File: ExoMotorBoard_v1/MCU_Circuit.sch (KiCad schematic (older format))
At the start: 12 parts, among them IC1 DSPIC33FJ128MC802-I_SP, J4 Conn_01x06_Male, SW1 SW_Push_Dual

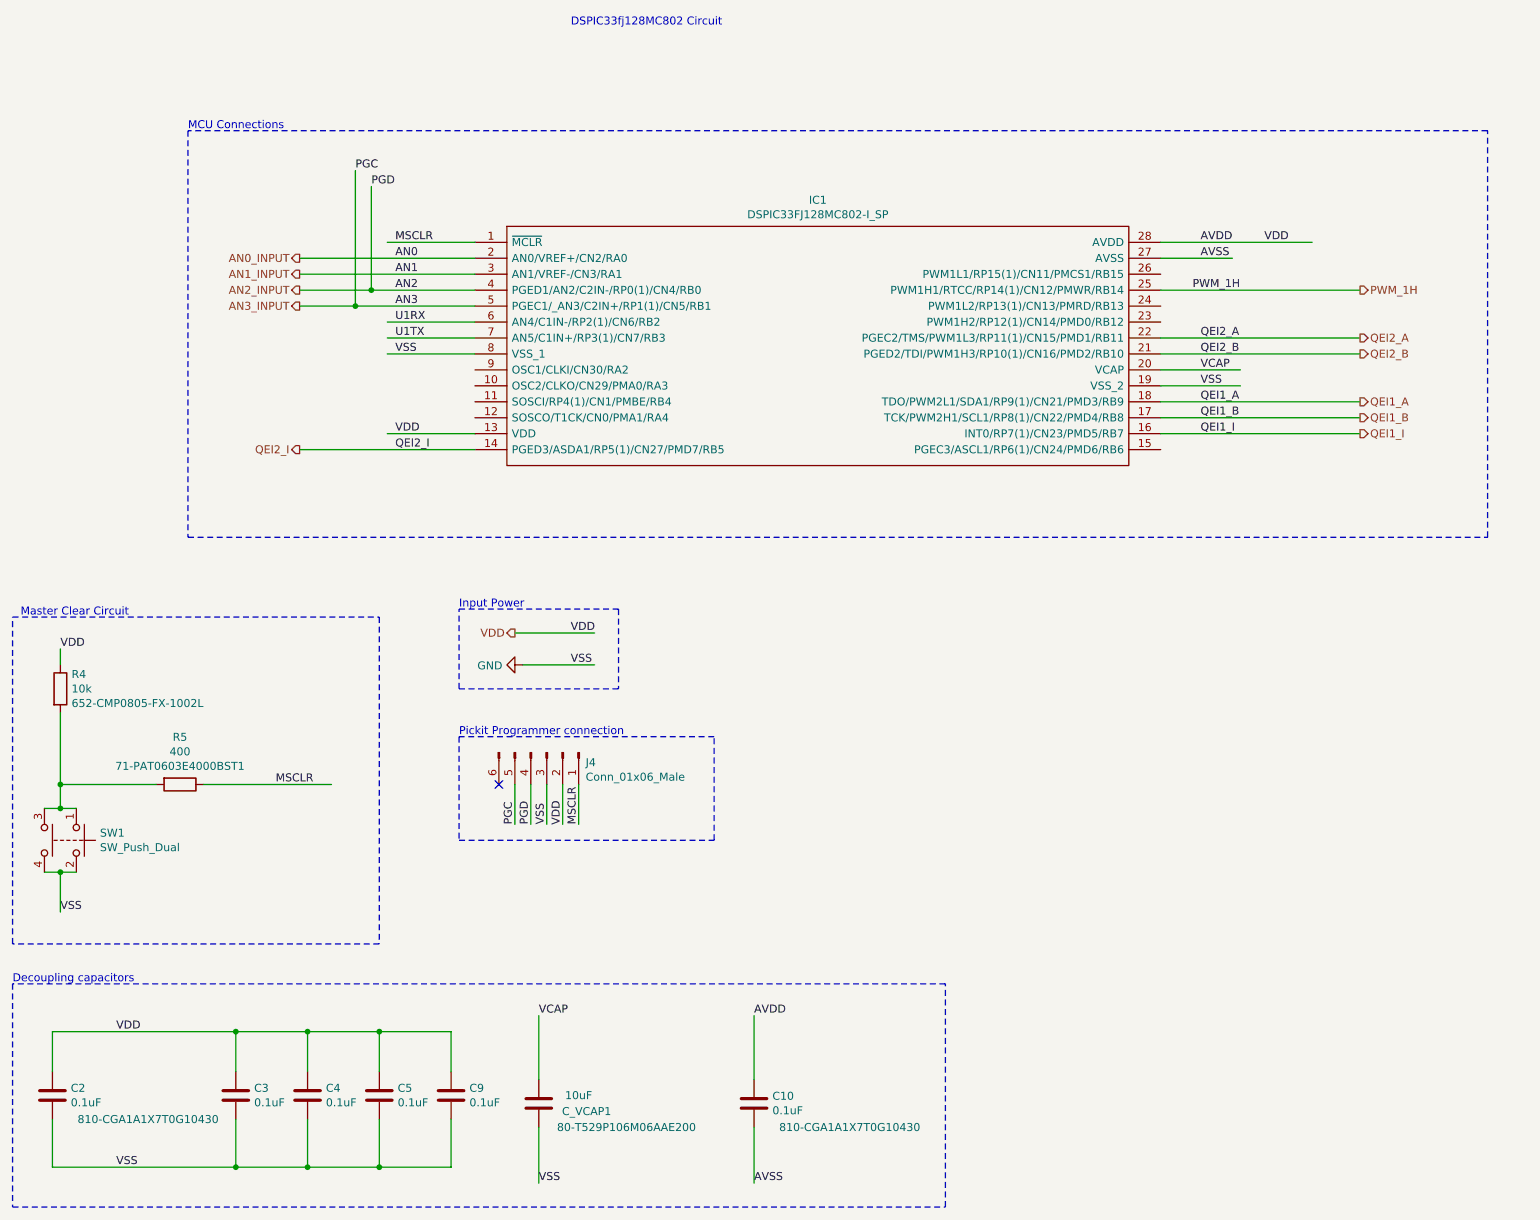
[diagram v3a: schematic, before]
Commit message: updated pins in the MCU circuit
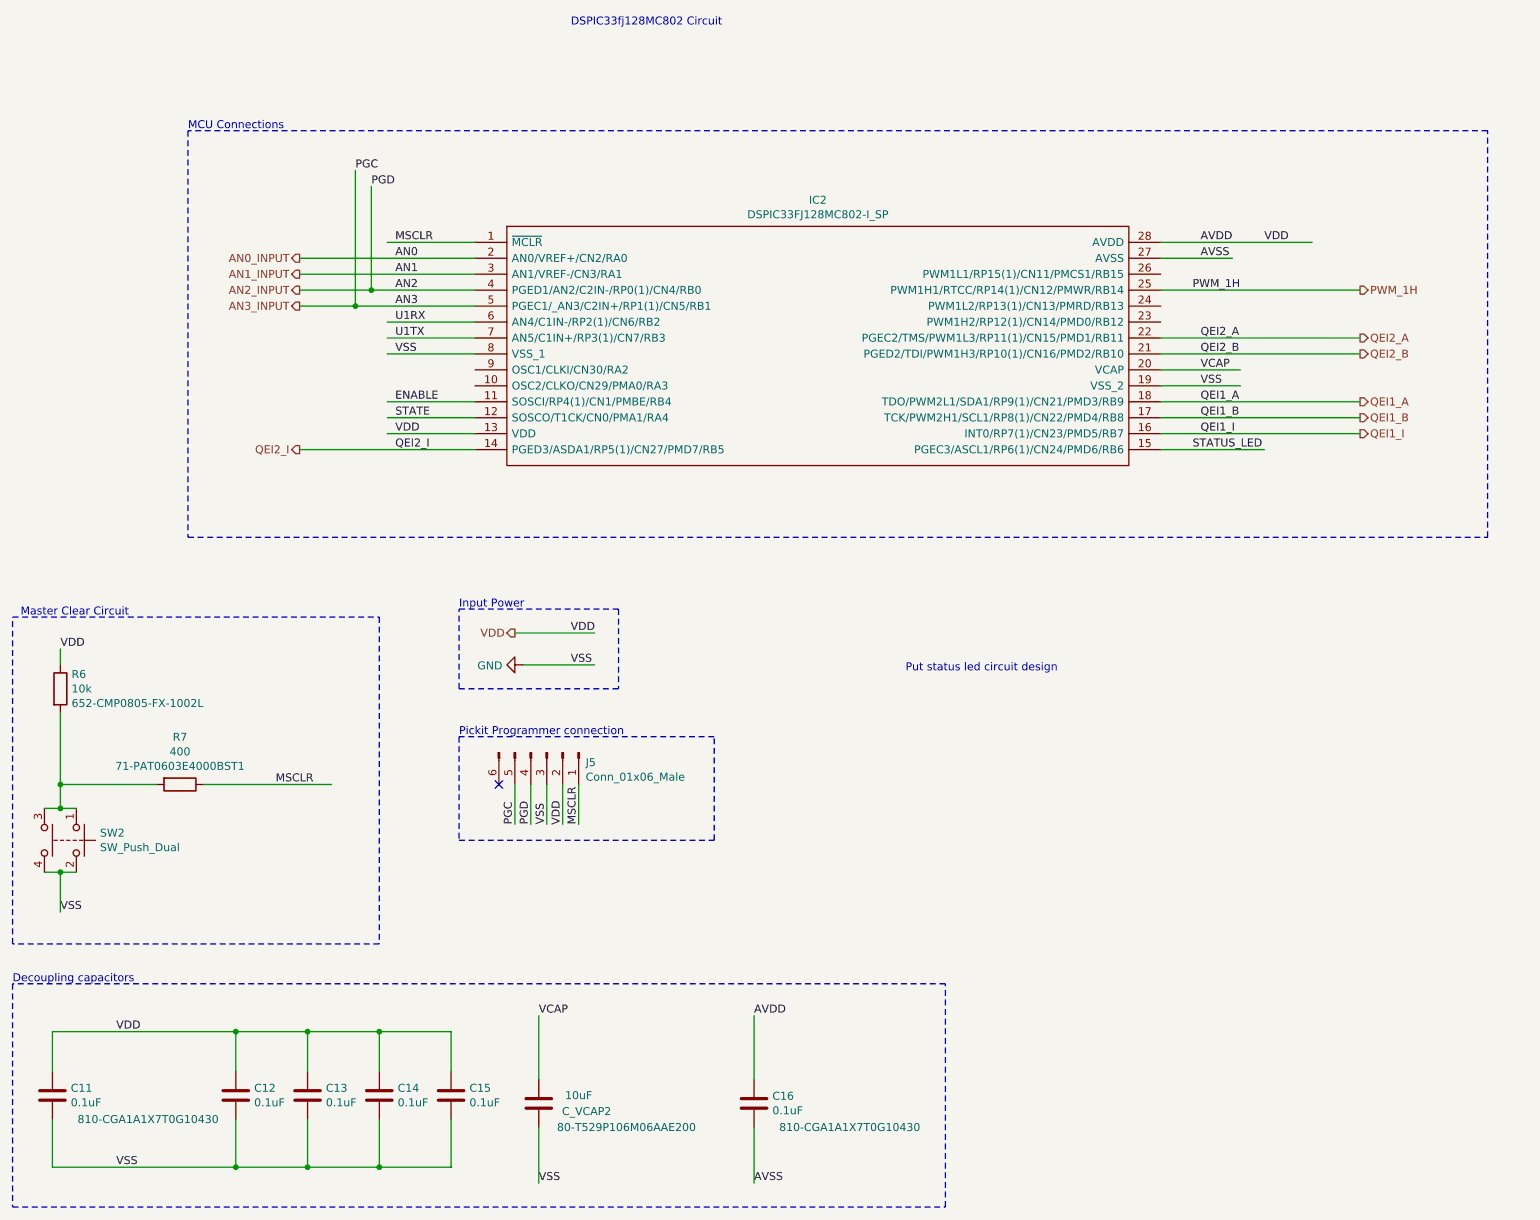
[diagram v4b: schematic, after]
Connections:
- net labels added: ENABLE, STATE, STATUS_LED
- wire segments 63 -> 66
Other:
- note added: "Put status led circuit design\n"
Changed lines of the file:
@@
 $Descr A4 11693 8268
 encoding utf-8
-Sheet 7 8
+Sheet 8 8
 Title ""
 Date ""
@@
 AR Path="/610E570F/610E8175" Ref="IC1"  Part="1"
 AR Path="/6118F320/610E8175" Ref="IC2"  Part="1"
-F 0 "IC1" H 5850 1815 50  0000 C CNN
+F 0 "IC2" H 5850 1815 50  0000 C CNN
 F 1 "DSPIC33FJ128MC802-I_SP" H 5850 1724 50  0000 C CNN
 F 2 "DSPIC33FJ128MC802-I_SP:DIP794W56P254L3486H508Q28N" H 7850 1650 50  0001 L CNN
@@
 AR Path="/610E570F/610E817B" Ref="C_VCAP1"  Part="1"
 AR Path="/6118F320/610E817B" Ref="C_VCAP2"  Part="1"
-F 0 "C_VCAP1" H 3800 7000 50  0000 C CNN
+F 0 "C_VCAP2" H 3800 7000 50  0000 C CNN
 F 1 "10uF" H 3850 6900 50  0000 C CNN
 F 2 "Capacitor_SMD:C_0805_2012Metric_Pad1.18x1.45mm_HandSolder" H 4138 6800 50  0001 C CNN
@@
 AR Path="/610E570F/610E818F" Ref="C2"  Part="1"
 AR Path="/6118F320/610E818F" Ref="C11"  Part="1"
-F 0 "C2" H 1165 6946 50  0000 L CNN
+F 0 "C11" H 1165 6946 50  0000 L CNN
 F 1 "0.1uF" H 1165 6855 50  0000 L CNN
 F 2 "Capacitor_SMD:C_0805_2012Metric_Pad1.18x1.45mm_HandSolder" H 1088 6750 50  0001 C CNN
@@
 AR Path="/610E570F/61167308" Ref="C3"  Part="1"
 AR Path="/6118F320/61167308" Ref="C12"  Part="1"
-F 0 "C3" H 2315 6946 50  0000 L CNN
+F 0 "C12" H 2315 6946 50  0000 L CNN
 F 1 "0.1uF" H 2315 6855 50  0000 L CNN
 F 2 "Capacitor_SMD:C_0805_2012Metric_Pad1.18x1.45mm_HandSolder" H 2238 6750 50  0001 C CNN
@@
 AR Path="/610E570F/611683F9" Ref="C4"  Part="1"
 AR Path="/6118F320/611683F9" Ref="C13"  Part="1"
-F 0 "C4" H 2765 6946 50  0000 L CNN
+F 0 "C13" H 2765 6946 50  0000 L CNN
 F 1 "0.1uF" H 2765 6855 50  0000 L CNN
 F 2 "Capacitor_SMD:C_0805_2012Metric_Pad1.18x1.45mm_HandSolder" H 2688 6750 50  0001 C CNN
@@
 AR Path="/610E570F/61168710" Ref="C5"  Part="1"
 AR Path="/6118F320/61168710" Ref="C14"  Part="1"
-F 0 "C5" H 3215 6946 50  0000 L CNN
+F 0 "C14" H 3215 6946 50  0000 L CNN
 F 1 "0.1uF" H 3215 6855 50  0000 L CNN
 F 2 "Capacitor_SMD:C_0805_2012Metric_Pad1.18x1.45mm_HandSolder" H 3138 6750 50  0001 C CNN
@@
 AR Path="/610E570F/61168A37" Ref="C9"  Part="1"
 AR Path="/6118F320/61168A37" Ref="C15"  Part="1"
-F 0 "C9" H 3665 6946 50  0000 L CNN
+F 0 "C15" H 3665 6946 50  0000 L CNN
 F 1 "0.1uF" H 3665 6855 50  0000 L CNN
 F 2 "Capacitor_SMD:C_0805_2012Metric_Pad1.18x1.45mm_HandSolder" H 3588 6750 50  0001 C CNN
@@
 AR Path="/610E570F/61184548" Ref="C10"  Part="1"
 AR Path="/6118F320/61184548" Ref="C16"  Part="1"
-F 0 "C10" H 5565 6996 50  0000 L CNN
+F 0 "C16" H 5565 6996 50  0000 L CNN
 F 1 "0.1uF" H 5565 6905 50  0000 L CNN
 F 2 "Capacitor_SMD:C_0805_2012Metric_Pad1.18x1.45mm_HandSolder" H 5488 6800 50  0001 C CNN
@@
 AR Path="/610E570F/611A7040" Ref="SW1"  Part="1"
 AR Path="/6118F320/611A7040" Ref="SW2"  Part="1"
-F 0 "SW1" V 1154 5448 50  0000 L CNN
+F 0 "SW2" V 1154 5448 50  0000 L CNN
 F 1 "SW_Push_Dual" V 1245 5448 50  0000 L CNN
 F 2 "Button_Switch_THT:SW_PUSH_6mm_H5mm" H 1200 5500 50  0001 C CNN
@@
 AR Path="/610E570F/611A34F1" Ref="R5"  Part="1"
 AR Path="/6118F320/611A34F1" Ref="R7"  Part="1"
-F 0 "R5" V 1553 4950 50  0000 C CNN
+F 0 "R7" V 1553 4950 50  0000 C CNN
 F 1 "400" V 1644 4950 50  0000 C CNN
 F 2 "Resistor_SMD:R_0603_1608Metric_Pad0.98x0.95mm_HandSolder" V 1780 4950 50  0001 C CNN
@@
 AR Path="/610E570F/611A30AE" Ref="R4"  Part="1"
 AR Path="/6118F320/611A30AE" Ref="R6"  Part="1"
-F 0 "R4" H 1170 4441 50  0000 L CNN
+F 0 "R6" H 1170 4441 50  0000 L CNN
 F 1 "10k" H 1170 4350 50  0000 L CNN
 F 2 "Resistor_SMD:R_0805_2012Metric_Pad1.20x1.40mm_HandSolder" V 1030 4350 50  0001 C CNN
@@
 AR Path="/610E570F/611C897C" Ref="#PWR0102"  Part="1"
 AR Path="/6118F320/611C897C" Ref="#PWR0104"  Part="1"
-F 0 "#PWR0102" H 4000 3950 50  0001 C CNN
+F 0 "#PWR0104" H 4000 3950 50  0001 C CNN
 F 1 "GND" V 4005 4072 50  0000 R CNN
 F 2 "" H 4000 4200 50  0001 C CNN
@@
 AR Path="/610E570F/611BB08D" Ref="J4"  Part="1"
 AR Path="/6118F320/611BB08D" Ref="J5"  Part="1"
-F 0 "J4" V 4212 4994 50  0000 L CNN
+F 0 "J5" V 4212 4994 50  0000 L CNN
 F 1 "Conn_01x06_Male" V 4303 4994 50  0000 L CNN
 F 2 "Connector_PinHeader_1.27mm:PinHeader_1x06_P1.27mm_Vertical" H 4150 4750 50  0001 C CNN
@@
 Text Label 3200 2150 0    50   ~ 0
 U1TX
+Text Label 8200 2850 0    50   ~ 0
+STATUS_LED
+Wire Wire Line
+	8000 2850 8650 2850
+Wire Wire Line
+	3700 2650 3150 2650
+Wire Wire Line
+	3700 2550 3150 2550
+Text Label 3200 2550 0    50   ~ 0
+ENABLE
+Text Label 3200 2650 0    50   ~ 0
+STATE
+Text Notes 6400 4250 0    50   ~ 0
+Put status led circuit design\n
 $EndSCHEMATC
